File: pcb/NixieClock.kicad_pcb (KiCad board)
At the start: 2 copper layers, 250 x 100 mm, 221 parts, among them J1 USB_B, J2 BARREL_JACK, J3 Screw_Terminal_1x04, Q1 MMBTA92, Q10 MMBTA92, Q11 MMBTA42, Q12 MMBTA42, Q13 MMBTA42, Q14 MMBTA42, Q15 MMBTA42, Q16 MMBTA42, Q17 MMBTA92, Q18 MMBTA42, Q19 MMBTA42, Q2 STD5N52U, Q20 MMBTA42, Q21 MMBTA92, Q22 MMBTA42, Q23 MMBTA42, Q24 MMBTA42, Q25 MMBTA42, Q26 MMBTA92, Q27 MMBTA42, Q28 MMBTA42, Q29 MMBTA42, Q3 MMBTA42, Q30 MMBTA92, Q31 MMBTA42, Q32 MMBTA42, Q33 MMBTA42, Q34 MMBTA42, Q35 MMBTA92, Q36 MMBTA42, Q37 MMBTA42, Q4 MMBTA42, Q5 MMBTA42, Q6 MMBTA42, Q7 MMBTA42, Q8 MMBTA42, Q9 MMBTA42, SW1 EG2219, SW2 SW_Push, SW3 SW_Push, SW4 SW_Push, SW5 SW_Push, SW6 SW_Push, SW7 SKQUCAA010, U1 DS3231, U10 MC34063A, U11 PCF8574, U12 PCF8574, U13 CD4028B, U14 74HC238, U15 74HC238, U16 74HC238, U2 PCF8574, U3 ESP-12F, U4 CH340G, U5 LM1117-3.3, U6 STA013, U7 CS4344, U8 PAM8403, U9 MC34063A, Y1 12MHz, Y2 12MHz

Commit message: Added notes to speaker output terminal block
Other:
- board text added: "+"
- board text added: "-"
- board text added: "L"
- board text added: "R"
- board text added: "speaker out"
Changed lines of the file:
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@@
     (area 22.197599 45.72 275.691601 150.266401)
     (thickness 1.6)
-    (drawings 12)
+    (drawings 19)
     (tracks 1594)
     (zones 0)
@@
     (pcbplotparams
       (layerselection 0x010f4_80000001)
-      (usegerberextensions false)
+      (usegerberextensions true)
       (excludeedgelayer true)
       (linewidth 0.100000)
@@
     (at 104.775 63.5)
     (descr "4-way 2.54mm pitch terminal block, Phoenix MPT series")
-    (fp_text reference J3 (at 3.81 -4.50088) (layer F.SilkS)
+    (fp_text reference J3 (at 10.16 0) (layer F.SilkS)
       (effects (font (size 1 1) (thickness 0.15)))
     )
@@
       (xy -0.381958 -9.244925) (xy -0.043769 -9.24521) (xy 0 -9.24521) (xy 0.348357 -9.245003)) (layer F.SilkS) (width 0.01))
   )
+  (gr_text "speaker out" (at 108.585 59.055) (layer F.SilkS)
+    (effects (font (size 1 1) (thickness 0.2)))
+  )
+  (gr_text R (at 111.125 69.85) (layer F.SilkS)
+    (effects (font (size 1.5 1.5) (thickness 0.3)))
+  )
+  (gr_text L (at 106.045 69.85) (layer F.SilkS)
+    (effects (font (size 1.5 1.5) (thickness 0.3)))
+  )
+  (gr_text - (at 112.395 67.945) (layer F.SilkS)
+    (effects (font (size 1.5 1.5) (thickness 0.3)))
+  )
+  (gr_text + (at 109.855 67.945) (layer F.SilkS)
+    (effects (font (size 1.5 1.5) (thickness 0.3)))
+  )
+  (gr_text - (at 107.315 67.945) (layer F.SilkS)
+    (effects (font (size 1.5 1.5) (thickness 0.3)))
+  )
+  (gr_text + (at 104.775 67.945) (layer F.SilkS)
+    (effects (font (size 1.5 1.5) (thickness 0.3)))
+  )
   (gr_text "Eigty-Two Nixie-Six\nNixie Tube Internet Radio Alam Clock\nDesigned by Austin R. Leydecker\nhttp://www.renkin42.net/\nAll documents hardware and sofware\nfreeely available from\nhttp://www.github.com/Renkin42/82Nix6/\nLicensed under MPL 2.0\nREV 1.0" (at 258.445 112.395 270) (layer F.SilkS)

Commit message: Use RTS and DTR for flashing instead of switch
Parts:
- removed the REF*** at (257.2, 125.1)
- removed SW1: EG2219, clock_footprints:EG2219
- added D4: MBR0520, Diodes_SMD:D_SOD-123, B.Cu at (124.5, 141.6)
- added Q38: MMBTA92, TO_SOT_Packages_SMD:SOT-23_Handsoldering, B.Cu at (129.5, 146.1)
- added R21: 10k, Resistors_SMD:R_0805_HandSoldering, B.Cu at (130.8, 141.6)
- added REF***: OSHW-Logo2_14.6x12mm_SilkScreen, Symbols:OSHW-Logo2_14.6x12mm_SilkScreen, F.Cu at (261.0, 121.9)
- moved R14 12.9 mm to (118.1, 139.1)
- moved C9 8.64 mm to (50.8, 82.5), turned to 180 degrees
- moved R15 7.22 mm to (118.1, 137.2), turned to 180 degrees
- moved C1 7.13 mm to (147.3, 121.9), turned to 270 degrees
- moved C6 4.07 mm to (144.8, 121.3), turned to 270 degrees
- moved R11 0.06 mm to (113.0, 146.1), turned to 180 degrees
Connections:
- C2 pad 1: Net-(C2-Pad1) -> USB_PWR
- C5 pad 1: Net-(C2-Pad1) -> USB_PWR
- C7 pad 1: USB_PWR -> Net-(C7-Pad1)
- R1 pad 1: +3V3 -> USB_PWR
- R1 pad 2: Net-(R1-Pad2) -> RST
- R11 pad 1: AMP_EN -> GND
- R11 pad 2: GND -> AMP_EN
- R14 pad 1: Net-(R14-Pad1) -> USB_PWR
- R14 pad 2: +3V3 -> Net-(R14-Pad2)
- R15 pad 1: Net-(R15-Pad1) -> USB_PWR
- R15 pad 2: +3V3 -> Net-(R15-Pad2)
- R2 pad 2: +3V3 -> USB_PWR
- SW2 pad 2: Net-(R1-Pad2) -> RST
- U3 pad 1: Net-(R1-Pad2) -> RST
- U3 pad 11: Net-(R14-Pad1) -> Net-(R14-Pad2)
- U3 pad 12: Net-(SW1-Pad5) -> Net-(R15-Pad2)
- U3 pad 8: Net-(C2-Pad1) -> USB_PWR
- U4 pad 13: Net-(U4-Pad13) -> Net-(R15-Pad2)
- U4 pad 14: Net-(U4-Pad14) -> RST
- U5 pad 2: USB_PWR -> Net-(C7-Pad1)
- U5 pad 4: USB_PWR -> Net-(C7-Pad1)
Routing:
- net RST: track 0.00 -> 131.0 mm, vias 0 -> 3
- net Net-(R1-Pad2): track 80.6 -> 0.00 mm, vias 1 -> 0
- net Net-(R15-Pad2): track 0.00 -> 45.9 mm, vias 0 -> 2
- net USB_PWR: track 79.8 -> 112.8 mm, vias 3 -> 7
- net Net-(C2-Pad1): track 31.4 -> 0.00 mm
- net Net-(SW1-Pad5): track 24.0 -> 0.00 mm
- net Net-(C7-Pad1): track 0.00 -> 9.63 mm
- net Net-(R14-Pad2): track 0.00 -> 9.36 mm
- net GND: track 4.41 -> 9.93 mm, vias 1 -> 3
- net Net-(R14-Pad1): track 5.02 -> 0.00 mm
- net Net-(R15-Pad1): track 4.24 -> 0.00 mm
- net +3V3: track 162.8 -> 159.3 mm, vias 35 -> 34
- net Net-(Q38-Pad1): track 0.00 -> 2.24 mm
- net +170V: track 548.5 -> 549.0 mm
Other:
- board text added: "Eigty-Two Nixie-Six Nixie Tube Internet Radio Alam Clock Designed by Austin R. Leydecker http://www.github.com/Renkin42/82Nix6/ Licensed under MPL 2.0 REV 1.1"
- board text removed: "+"
- board text removed: "-"
- board text removed: "Eigty-Two Nixie-Six Nixie Tube Internet Radio Alam Clock Designed by Austin R. Leydecker http://www.renkin42.net/ All documents hardware and sofware freeely available from http://www.github.com/Renkin42/82Nix6/ Licensed under MPL 2.0 REV 1.0"
- board text removed: "L"
- board text removed: "R"
- board text removed: "speaker out"

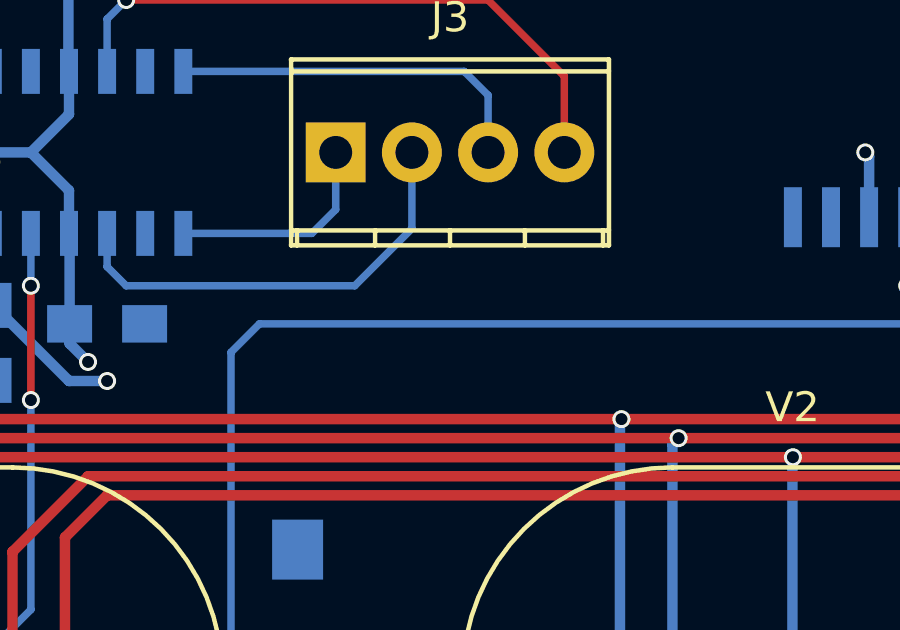
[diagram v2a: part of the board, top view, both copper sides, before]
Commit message: Added model for ESP12. Updated schematic exports.
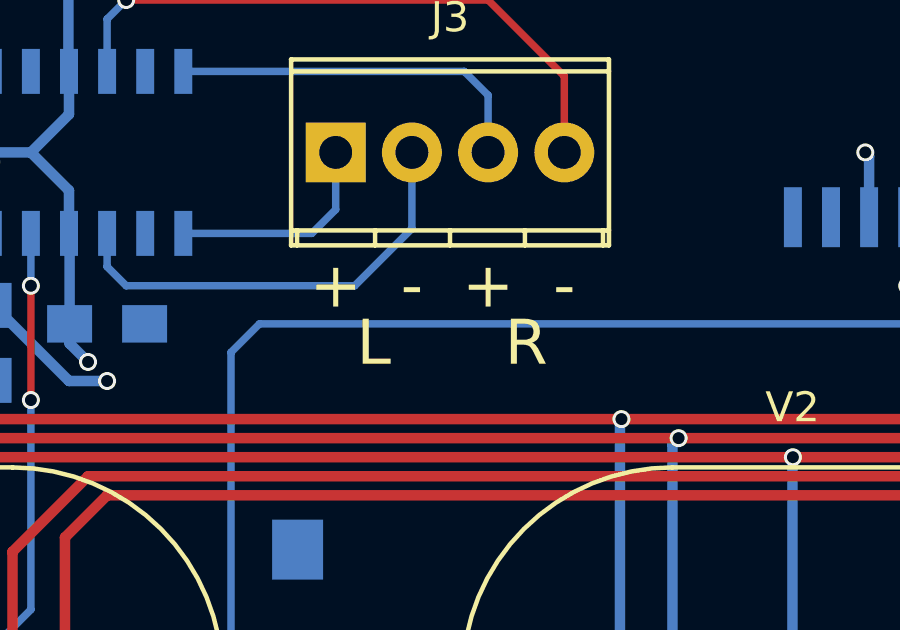
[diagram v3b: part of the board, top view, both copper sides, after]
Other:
- board text added: "+"
- board text added: "-"
- board text added: "L"
- board text added: "R"
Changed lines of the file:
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@@
     (area 22.197599 45.72 275.691601 150.266401)
     (thickness 1.6)
-    (drawings 12)
+    (drawings 18)
     (tracks 1637)
     (zones 0)
@@
     )
   )
-  (module clock_footprints:ESP_SMD_Module (layer B.Cu)
-    (at 114.76736 132.78866 270)
-    (fp_text reference U3 (at 0 -1.778 270) (layer B.SilkS)
-      (effects (font (size 1 1) (thickness 0.15)) (justify mirror))
-    )
-    (fp_text value ESP-12F (at 0 6.604 270) (layer B.Fab)
-      (effects (font (size 1 1) (thickness 0.15)) (justify mirror))
-    )
-    (fp_line (start 6.5 20.5) (end 6.5 18) (layer B.SilkS) (width 0.15))
-    (fp_line (start -3.5 22.5) (end -1.5 22.5) (layer B.SilkS) (width 0.15))
-    (fp_line (start -1.5 22.5) (end -1.5 20.5) (layer B.SilkS) (width 0.15))
-    (fp_line (start -1.5 20.5) (end 0.5 20.5) (layer B.SilkS) (width 0.15))
-    (fp_line (start 0.5 20.5) (end 0.5 22.5) (layer B.SilkS) (width 0.15))
-    (fp_line (start 0.5 22.5) (end 2.5 22.5) (layer B.SilkS) (width 0.15))
-    (fp_line (start 2.5 22.5) (end 2.5 20.5) (layer B.SilkS) (width 0.15))
-    (fp_line (start 2.5 20.5) (end 4.5 20.5) (layer B.SilkS) (width 0.15))
-    (fp_line (start 4.5 20.5) (end 4.5 22.5) (layer B.SilkS) (width 0.15))
-    (fp_line (start 4.5 22.5) (end 6.5 22.5) (layer B.SilkS) (width 0.15))
-    (fp_line (start 6.5 22.5) (end 6.5 20.5) (layer B.SilkS) (width 0.15))
-    (fp_line (start -6 17) (end -6 22.5) (layer B.SilkS) (width 0.15))
-    (fp_line (start -6 22.5) (end -3.5 22.5) (layer B.SilkS) (width 0.15))
-    (fp_line (start -3.5 22.5) (end -3.5 17) (layer B.SilkS) (width 0.15))
-    (fp_line (start 8 24) (end 8 17) (layer B.SilkS) (width 0.15))
-    (fp_line (start -8 24) (end -8 17) (layer B.SilkS) (width 0.15))
-    (fp_line (start -8 23.98005) (end 8 23.98005) (layer B.SilkS) (width 0.15))
-    (fp_line (start -8 0) (end 8 0) (layer B.SilkS) (width 0.15))
-    (pad 1 smd rect (at -8.5 15.48 270) (size 3 1) (layers B.Cu B.Paste B.Mask)
-      (net 215 RST))
-    (pad 2 smd rect (at -8.5 13.48 270) (size 3 1) (layers B.Cu B.Paste B.Mask)
-      (net 168 "Net-(U3-Pad2)"))
-    (pad 3 smd rect (at -8.5 11.48 270) (size 3 1) (layers B.Cu B.Paste B.Mask)
-      (net 116 "Net-(R2-Pad1)"))
-    (pad 4 smd rect (at -8.5 9.48 270) (size 3 1) (layers B.Cu B.Paste B.Mask)
-      (net 169 DREQ))
-    (pad 5 smd rect (at -8.5 7.48 270) (size 3 1) (layers B.Cu B.Paste B.Mask)
-      (net 170 MOSI))
-    (pad 6 smd rect (at -8.5 5.48 270) (size 3 1) (layers B.Cu B.Paste B.Mask)
-      (net 171 "Net-(U3-Pad6)"))
-    (pad 7 smd rect (at -8.5 3.48 270) (size 3 1) (layers B.Cu B.Paste B.Mask)
-      (net 172 SCK))
-    (pad 8 smd rect (at -8.5 1.48 270) (size 3 1) (layers B.Cu B.Paste B.Mask)
-      (net 5 USB_PWR))
-    (pad 9 smd rect (at 8.5 1.48 270) (size 3 1) (layers B.Cu B.Paste B.Mask)
-      (net 2 GND))
-    (pad 10 smd rect (at 8.5 3.48 270) (size 3 1) (layers B.Cu B.Paste B.Mask)
-      (net 125 AMP_EN))
-    (pad 11 smd rect (at 8.5 5.48 270) (size 3 1) (layers B.Cu B.Paste B.Mask)
-      (net 216 "Net-(R14-Pad2)"))
-    (pad 12 smd rect (at 8.5 7.48 270) (size 3 1) (layers B.Cu B.Paste B.Mask)
-      (net 217 "Net-(R15-Pad2)"))
-    (pad 13 smd rect (at 8.5 9.48 270) (size 3 1) (layers B.Cu B.Paste B.Mask)
-      (net 127 SDA))
-    (pad 14 smd rect (at 8.5 11.48 270) (size 3 1) (layers B.Cu B.Paste B.Mask)
-      (net 126 SCL))
-    (pad 15 smd rect (at 8.5 13.48 270) (size 3 1) (layers B.Cu B.Paste B.Mask)
-      (net 129 Rx))
-    (pad 16 smd rect (at 8.5 15.48 270) (size 3 1) (layers B.Cu B.Paste B.Mask)
-      (net 131 Tx))
-  )
   (module Housings_SOIC:SOIC-16_3.9x9.9mm_Pitch1.27mm (layer B.Cu)
     (at 137.795 120.396 90)
@@
     (pad "" np_thru_hole circle (at 0 0) (size 4.5 4.5) (drill 4.5) (layers *.Cu *.Mask))
   )
+  (module clock_footprints:ESP_SMD_Module (layer B.Cu)
+    (at 114.76736 132.78866 270)
+    (fp_text reference U3 (at 0 -1.778 270) (layer B.SilkS)
+      (effects (font (size 1 1) (thickness 0.15)) (justify mirror))
+    )
+    (fp_text value ESP-12F (at 0 6.604 270) (layer B.Fab)
+      (effects (font (size 1 1) (thickness 0.15)) (justify mirror))
+    )
+    (fp_line (start 6.5 20.5) (end 6.5 18) (layer B.SilkS) (width 0.15))
+    (fp_line (start -3.5 22.5) (end -1.5 22.5) (layer B.SilkS) (width 0.15))
+    (fp_line (start -1.5 22.5) (end -1.5 20.5) (layer B.SilkS) (width 0.15))
+    (fp_line (start -1.5 20.5) (end 0.5 20.5) (layer B.SilkS) (width 0.15))
+    (fp_line (start 0.5 20.5) (end 0.5 22.5) (layer B.SilkS) (width 0.15))
+    (fp_line (start 0.5 22.5) (end 2.5 22.5) (layer B.SilkS) (width 0.15))
+    (fp_line (start 2.5 22.5) (end 2.5 20.5) (layer B.SilkS) (width 0.15))
+    (fp_line (start 2.5 20.5) (end 4.5 20.5) (layer B.SilkS) (width 0.15))
+    (fp_line (start 4.5 20.5) (end 4.5 22.5) (layer B.SilkS) (width 0.15))
+    (fp_line (start 4.5 22.5) (end 6.5 22.5) (layer B.SilkS) (width 0.15))
+    (fp_line (start 6.5 22.5) (end 6.5 20.5) (layer B.SilkS) (width 0.15))
+    (fp_line (start -6 17) (end -6 22.5) (layer B.SilkS) (width 0.15))
+    (fp_line (start -6 22.5) (end -3.5 22.5) (layer B.SilkS) (width 0.15))
+    (fp_line (start -3.5 22.5) (end -3.5 17) (layer B.SilkS) (width 0.15))
+    (fp_line (start 8 24) (end 8 17) (layer B.SilkS) (width 0.15))
+    (fp_line (start -8 24) (end -8 17) (layer B.SilkS) (width 0.15))
+    (fp_line (start -8 23.98005) (end 8 23.98005) (layer B.SilkS) (width 0.15))
+    (fp_line (start -8 0) (end 8 0) (layer B.SilkS) (width 0.15))
+    (pad 1 smd rect (at -8.5 15.48 270) (size 3 1) (layers B.Cu B.Paste B.Mask)
+      (net 215 RST))
+    (pad 2 smd rect (at -8.5 13.48 270) (size 3 1) (layers B.Cu B.Paste B.Mask)
+      (net 168 "Net-(U3-Pad2)"))
+    (pad 3 smd rect (at -8.5 11.48 270) (size 3 1) (layers B.Cu B.Paste B.Mask)
+      (net 116 "Net-(R2-Pad1)"))
+    (pad 4 smd rect (at -8.5 9.48 270) (size 3 1) (layers B.Cu B.Paste B.Mask)
+      (net 169 DREQ))
+    (pad 5 smd rect (at -8.5 7.48 270) (size 3 1) (layers B.Cu B.Paste B.Mask)
+      (net 170 MOSI))
+    (pad 6 smd rect (at -8.5 5.48 270) (size 3 1) (layers B.Cu B.Paste B.Mask)
+      (net 171 "Net-(U3-Pad6)"))
+    (pad 7 smd rect (at -8.5 3.48 270) (size 3 1) (layers B.Cu B.Paste B.Mask)
+      (net 172 SCK))
+    (pad 8 smd rect (at -8.5 1.48 270) (size 3 1) (layers B.Cu B.Paste B.Mask)
+      (net 5 USB_PWR))
+    (pad 9 smd rect (at 8.5 1.48 270) (size 3 1) (layers B.Cu B.Paste B.Mask)
+      (net 2 GND))
+    (pad 10 smd rect (at 8.5 3.48 270) (size 3 1) (layers B.Cu B.Paste B.Mask)
+      (net 125 AMP_EN))
+    (pad 11 smd rect (at 8.5 5.48 270) (size 3 1) (layers B.Cu B.Paste B.Mask)
+      (net 216 "Net-(R14-Pad2)"))
+    (pad 12 smd rect (at 8.5 7.48 270) (size 3 1) (layers B.Cu B.Paste B.Mask)
+      (net 217 "Net-(R15-Pad2)"))
+    (pad 13 smd rect (at 8.5 9.48 270) (size 3 1) (layers B.Cu B.Paste B.Mask)
+      (net 127 SDA))
+    (pad 14 smd rect (at 8.5 11.48 270) (size 3 1) (layers B.Cu B.Paste B.Mask)
+      (net 126 SCL))
+    (pad 15 smd rect (at 8.5 13.48 270) (size 3 1) (layers B.Cu B.Paste B.Mask)
+      (net 129 Rx))
+    (pad 16 smd rect (at 8.5 15.48 270) (size 3 1) (layers B.Cu B.Paste B.Mask)
+      (net 131 Tx))
+    (model ${KIPRJMOD}/clock_footprints_3d/ESPModule.wrl
+      (at (xyz 0 0 0))
+      (scale (xyz 0.3937008 0.3937008 0.3937008))
+      (rotate (xyz 0 0 0))
+    )
+  )
+  (gr_text R (at 111.125 69.85) (layer F.SilkS)
+    (effects (font (size 1.5 1.5) (thickness 0.3)))
+  )
+  (gr_text L (at 106.045 69.85) (layer F.SilkS)
+    (effects (font (size 1.5 1.5) (thickness 0.3)))
+  )
+  (gr_text - (at 112.395 67.945) (layer F.SilkS)
+    (effects (font (size 1.5 1.5) (thickness 0.3)))
+  )
+  (gr_text + (at 109.855 67.945) (layer F.SilkS)
+    (effects (font (size 1.5 1.5) (thickness 0.3)))
+  )
+  (gr_text - (at 107.315 67.945) (layer F.SilkS)
+    (effects (font (size 1.5 1.5) (thickness 0.3)))
+  )
+  (gr_text + (at 104.775 67.945) (layer F.SilkS)
+    (effects (font (size 1.5 1.5) (thickness 0.3)))
+  )
   (gr_text "Eigty-Two Nixie-Six\nNixie Tube Internet Radio Alam Clock\nDesigned by Austin R. Leydecker\nhttp://www.github.com/Renkin42/82Nix6/\nLicensed under MPL 2.0\nREV 1.1" (at 260.985 113.665 270) (layer F.SilkS)
     (effects (font (size 1.5 1.5) (thickness 0.3)) (justify right))
@@
   (segment (start 142.4432 133.7056) (end 146.1704 133.7056) (width 0.35) (layer B.Cu) (net 6))
   (segment (start 146.1704 133.7056) (end 146.304 133.572) (width 0.35) (layer B.Cu) (net 6))
-  (segment (start 52.05 82.55) (end 52.05 84.435) (width 0.35) (layer B.Cu) (net 7) (status 400000))
+  (segment (start 52.05 82.55) (end 52.05 84.435) (width 0.35) (layer B.Cu) (net 7))
   (via (at 52.07 84.455) (size 0.6) (drill 0.4) (layers F.Cu B.Cu) (net 7))
   (segment (start 52.05 84.435) (end 52.07 84.455) (width 0.35) (layer B.Cu) (net 7))

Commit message: Switched to nodemcu-style flashing circuitry.
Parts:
- removed the REF*** at (261.0, 121.9)
- removed SW6: SW_Push, Buttons_Switches_THT:SW_Tactile_SKHH_Angled
- removed SW7: SKQUCAA010, clock_footprints:SKQUCAA010
- added Q39: MMBT3904, TO_SOT_Packages_SMD:SOT-23_Handsoldering, B.Cu at (132.7, 108.0)
- added Q40: MMBT3904, TO_SOT_Packages_SMD:SOT-23_Handsoldering, B.Cu at (132.7, 111.8)
- added R22: 10k, Resistors_SMD:R_0805_HandSoldering, B.Cu at (136.5, 109.2)
- added R90: 10k, Resistors_SMD:R_0805_HandSoldering, B.Cu at (130.8, 141.6)
- added REF**: Symbol_HighVoltage_Type2_CopperTop_VerySmall, clock_footprints:Symbol_HighVoltage_Type2_FSilkS_VerySmall, F.Cu at (255.9, 111.1)
- added REF***: OSHW-Logo_7.5x8mm_SilkScreen, Symbols:OSHW-Logo_7.5x8mm_SilkScreen, F.Cu at (245.7, 110.5)
- added SW1: SKQUCAA010, clock_footprints:SKQUCAA010, F.Cu at (240.7, 125.1)
- Q1: value MMBTA92 -> MMBT3906
- Q38: value MMBTA92 -> Si2301CDS
- SW2: footprint Buttons_Switches_THT:SW_Tactile_SKHH_Angled -> Buttons_Switches_THT:SW_PUSH_6mm
- SW4: footprint Buttons_Switches_THT:SW_PUSH_6mm -> Buttons_Switches_THT:SW_Tactile_SKHH_Angled
- moved SW2 163.6 mm to (191.8, 118.1), turned to 0 degrees
- moved SW4 86.6 mm to (219.7, 53.3), turned to 180 degrees
- moved R21 31.2 mm to (128.9, 110.5)
- moved SW3 29.8 mm to (161.9, 118.1)
- moved C1 9.44 mm to (144.1, 113.0), turned to 0 degrees
- moved C6 5.85 mm to (143.5, 115.6), turned to 0 degrees
- turned R1 to 90 degrees
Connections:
- R1 pad 1: USB_PWR -> RESET
- R1 pad 2: RST -> USB_PWR
- R12 pad 1: +3V3 -> USB_PWR
- R13 pad 1: +3V3 -> USB_PWR
- R15 pad 2: Net-(R15-Pad2) -> GPIO0
- R21 pad 1: Net-(Q38-Pad1) -> DTR
- R21 pad 2: +3V3 -> Net-(Q39-Pad1)
- SW2 pad 1: GND -> Net-(R5-Pad2)
- SW2 pad 2: RST -> GND
- SW3 pad 1: Net-(R5-Pad2) -> Net-(R4-Pad2)
- SW4 pad 1: Net-(R4-Pad2) -> Net-(R3-Pad2)
- U1 pad 2: +3V3 -> USB_PWR
- U1 pad 4: +3V3 -> USB_PWR
- U3 pad 1: RST -> RESET
- U3 pad 12: Net-(R15-Pad2) -> GPIO0
- U4 pad 13: Net-(R15-Pad2) -> DTR
- U4 pad 14: RST -> RTS
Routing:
- net RST: track 131.0 -> 0.00 mm, vias 3 -> 0
- net USB_PWR: track 112.8 -> 185.5 mm, vias 7 -> 10
- net RESET: track 0.00 -> 55.3 mm, vias 0 -> 2
- net GPIO0: track 0.00 -> 46.0 mm, vias 0 -> 2
- net Net-(R15-Pad2): track 45.9 -> 0.00 mm, vias 2 -> 0
- net +170V: track 549.0 -> 526.4 mm, vias 15 -> 14
- net DTR: track 0.00 -> 14.2 mm
- net RTS: track 0.00 -> 14.2 mm
- net GND: track 9.93 -> 17.1 mm, vias 3 -> 7
- net +3V3: track 159.3 -> 155.5 mm, vias 34 -> 32
- net Net-(Q40-Pad1): track 0.00 -> 2.41 mm
- net Net-(Q39-Pad1): track 0.00 -> 2.41 mm
- net Net-(D2-Pad1): track 18.5 -> 19.2 mm
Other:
- board text added: "Eigty-Two Nixie-Six By Austin R. Leydecker https://git.io/v9fmR Licensed under MPL 2.0 REV 1.1"
- board text removed: "Eigty-Two Nixie-Six Nixie Tube Internet Radio Alam Clock Designed by Austin R. Leydecker http://www.github.com/Renkin42/82Nix6/ Licensed under MPL 2.0 REV 1.1"
